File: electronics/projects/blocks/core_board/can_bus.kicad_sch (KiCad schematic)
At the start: 8 parts, among them U801 TCAN330DR

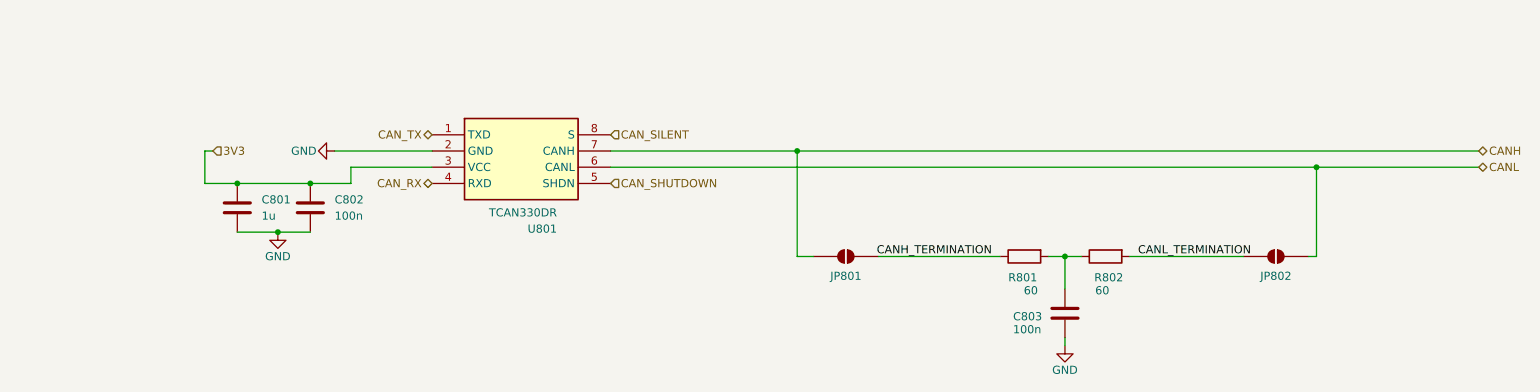
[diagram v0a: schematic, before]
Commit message: Update all sheets in core board project. Still looking for processes that give the cleanest update of a design block to a target board design.
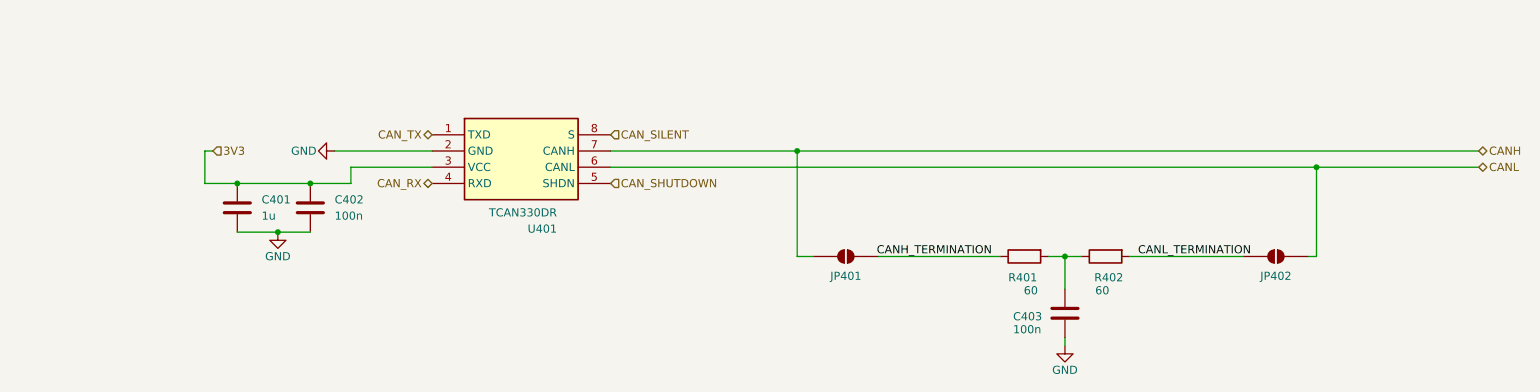
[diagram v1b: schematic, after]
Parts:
- renumbered C801 to C401, C802 to C402, C803 to C403, JP801 to JP401, JP802 to JP402, R801 to R401, R802 to R402, U801 to U401
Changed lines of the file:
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@@
 		(in_pos_files yes)
 		(dnp no)
-		(property "Reference" "C803"
+		(property "Reference" "C403"
 			(at 173.228 77.978 0)
 			(show_name no)
@@
 			)
 			(project "core_board"
-				(path "/efde0c74-5be6-4589-ad87-b4823ac1634b/c87fd2a4-f8d6-4149-89ef-17a7a7e4f014/68c0cd51-7ed2-4766-8be8-a243f7151f10"
-					(reference "C803")
+				(path "/efde0c74-5be6-4589-ad87-b4823ac1634b/c87fd2a4-f8d6-4149-89ef-17a7a7e4f014/66e88cae-c705-41c6-a86f-41a4af975dfd"
+					(reference "C403")
 					(unit 1)
 				)
@@
 		(in_pos_files yes)
 		(dnp no)
-		(property "Reference" "U801"
+		(property "Reference" "U401"
 			(at 99.568 64.262 0)
 			(show_name no)
@@
 			)
 			(project "core_board"
-				(path "/efde0c74-5be6-4589-ad87-b4823ac1634b/c87fd2a4-f8d6-4149-89ef-17a7a7e4f014/68c0cd51-7ed2-4766-8be8-a243f7151f10"
-					(reference "U801")
+				(path "/efde0c74-5be6-4589-ad87-b4823ac1634b/c87fd2a4-f8d6-4149-89ef-17a7a7e4f014/66e88cae-c705-41c6-a86f-41a4af975dfd"
+					(reference "U401")
 					(unit 1)
 				)
@@
 		(in_pos_files yes)
 		(dnp no)
-		(property "Reference" "R802"
+		(property "Reference" "R402"
 			(at 185.928 71.882 90)
 			(show_name no)
@@
 			)
 			(project "core_board"
-				(path "/efde0c74-5be6-4589-ad87-b4823ac1634b/c87fd2a4-f8d6-4149-89ef-17a7a7e4f014/68c0cd51-7ed2-4766-8be8-a243f7151f10"
-					(reference "R802")
+				(path "/efde0c74-5be6-4589-ad87-b4823ac1634b/c87fd2a4-f8d6-4149-89ef-17a7a7e4f014/66e88cae-c705-41c6-a86f-41a4af975dfd"
+					(reference "R402")
 					(unit 1)
 				)
@@
 		(in_pos_files yes)
 		(dnp no)
-		(property "Reference" "#PWR0802"
+		(property "Reference" "#PWR0402"
 			(at 58.42 52.07 0)
 			(hide yes)
@@
 			)
 			(project "core_board"
-				(path "/efde0c74-5be6-4589-ad87-b4823ac1634b/c87fd2a4-f8d6-4149-89ef-17a7a7e4f014/68c0cd51-7ed2-4766-8be8-a243f7151f10"
-					(reference "#PWR0802")
+				(path "/efde0c74-5be6-4589-ad87-b4823ac1634b/c87fd2a4-f8d6-4149-89ef-17a7a7e4f014/66e88cae-c705-41c6-a86f-41a4af975dfd"
+					(reference "#PWR0402")
 					(unit 1)
 				)
@@
 		(in_pos_files yes)
 		(dnp no)
-		(property "Reference" "JP801"
+		(property "Reference" "JP401"
 			(at 144.78 72.39 0)
 			(show_name no)
@@
 			)
 			(project "core_board"
-				(path "/efde0c74-5be6-4589-ad87-b4823ac1634b/c87fd2a4-f8d6-4149-89ef-17a7a7e4f014/68c0cd51-7ed2-4766-8be8-a243f7151f10"
-					(reference "JP801")
+				(path "/efde0c74-5be6-4589-ad87-b4823ac1634b/c87fd2a4-f8d6-4149-89ef-17a7a7e4f014/66e88cae-c705-41c6-a86f-41a4af975dfd"
+					(reference "JP401")
 					(unit 1)
 				)
@@
 		(in_pos_files yes)
 		(dnp no)
-		(property "Reference" "#PWR0801"
+		(property "Reference" "#PWR0401"
 			(at 55.88 71.12 0)
 			(hide yes)
@@
 			)
 			(project "core_board"
-				(path "/efde0c74-5be6-4589-ad87-b4823ac1634b/c87fd2a4-f8d6-4149-89ef-17a7a7e4f014/68c0cd51-7ed2-4766-8be8-a243f7151f10"
-					(reference "#PWR0801")
+				(path "/efde0c74-5be6-4589-ad87-b4823ac1634b/c87fd2a4-f8d6-4149-89ef-17a7a7e4f014/66e88cae-c705-41c6-a86f-41a4af975dfd"
+					(reference "#PWR0401")
 					(unit 1)
 				)
@@
 		(in_pos_files yes)
 		(dnp no)
-		(property "Reference" "#PWR0803"
+		(property "Reference" "#PWR0403"
 			(at 179.07 88.9 0)
 			(hide yes)
@@
 			)
 			(project "core_board"
-				(path "/efde0c74-5be6-4589-ad87-b4823ac1634b/c87fd2a4-f8d6-4149-89ef-17a7a7e4f014/68c0cd51-7ed2-4766-8be8-a243f7151f10"
-					(reference "#PWR0803")
+				(path "/efde0c74-5be6-4589-ad87-b4823ac1634b/c87fd2a4-f8d6-4149-89ef-17a7a7e4f014/66e88cae-c705-41c6-a86f-41a4af975dfd"
+					(reference "#PWR0403")
 					(unit 1)
 				)
@@
 		(in_pos_files yes)
 		(dnp no)
-		(property "Reference" "JP802"
+		(property "Reference" "JP402"
 			(at 212.09 72.39 0)
 			(show_name no)
@@
 			)
 			(project "core_board"
-				(path "/efde0c74-5be6-4589-ad87-b4823ac1634b/c87fd2a4-f8d6-4149-89ef-17a7a7e4f014/68c0cd51-7ed2-4766-8be8-a243f7151f10"
-					(reference "JP802")
+				(path "/efde0c74-5be6-4589-ad87-b4823ac1634b/c87fd2a4-f8d6-4149-89ef-17a7a7e4f014/66e88cae-c705-41c6-a86f-41a4af975dfd"
+					(reference "JP402")
 					(unit 1)
 				)
@@
 		(dnp no)
 		(fields_autoplaced yes)
-		(property "Reference" "C802"
+		(property "Reference" "C402"
 			(at 64.77 59.69 0)
 			(show_name no)
@@
 			)
 			(project "core_board"
-				(path "/efde0c74-5be6-4589-ad87-b4823ac1634b/c87fd2a4-f8d6-4149-89ef-17a7a7e4f014/68c0cd51-7ed2-4766-8be8-a243f7151f10"
-					(reference "C802")
+				(path "/efde0c74-5be6-4589-ad87-b4823ac1634b/c87fd2a4-f8d6-4149-89ef-17a7a7e4f014/66e88cae-c705-41c6-a86f-41a4af975dfd"
+					(reference "C402")
 					(unit 1)
 				)
@@
 		(in_pos_files yes)
 		(dnp no)
-		(property "Reference" "R801"
+		(property "Reference" "R401"
 			(at 172.466 71.882 90)
 			(show_name no)
@@
 			)
 			(project "core_board"
-				(path "/efde0c74-5be6-4589-ad87-b4823ac1634b/c87fd2a4-f8d6-4149-89ef-17a7a7e4f014/68c0cd51-7ed2-4766-8be8-a243f7151f10"
-					(reference "R801")
+				(path "/efde0c74-5be6-4589-ad87-b4823ac1634b/c87fd2a4-f8d6-4149-89ef-17a7a7e4f014/66e88cae-c705-41c6-a86f-41a4af975dfd"
+					(reference "R401")
 					(unit 1)
 				)
@@
 		(dnp no)
 		(fields_autoplaced yes)
-		(property "Reference" "C801"
+		(property "Reference" "C401"
 			(at 53.34 59.69 0)
 			(show_name no)
@@
 			)
 			(project "core_board"
-				(path "/efde0c74-5be6-4589-ad87-b4823ac1634b/c87fd2a4-f8d6-4149-89ef-17a7a7e4f014/68c0cd51-7ed2-4766-8be8-a243f7151f10"
-					(reference "C801")
-					(unit 1)
-				)
+				(path "/efde0c74-5be6-4589-ad87-b4823ac1634b/c87fd2a4-f8d6-4149-89ef-17a7a7e4f014/66e88cae-c705-41c6-a86f-41a4af975dfd"
+					(reference "C401")
+					(unit 1)
+				)

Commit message: Get core board schematic and layout to pass ERC and DRC. Rework layout to improve organization of components while allowing for future reuse of design.
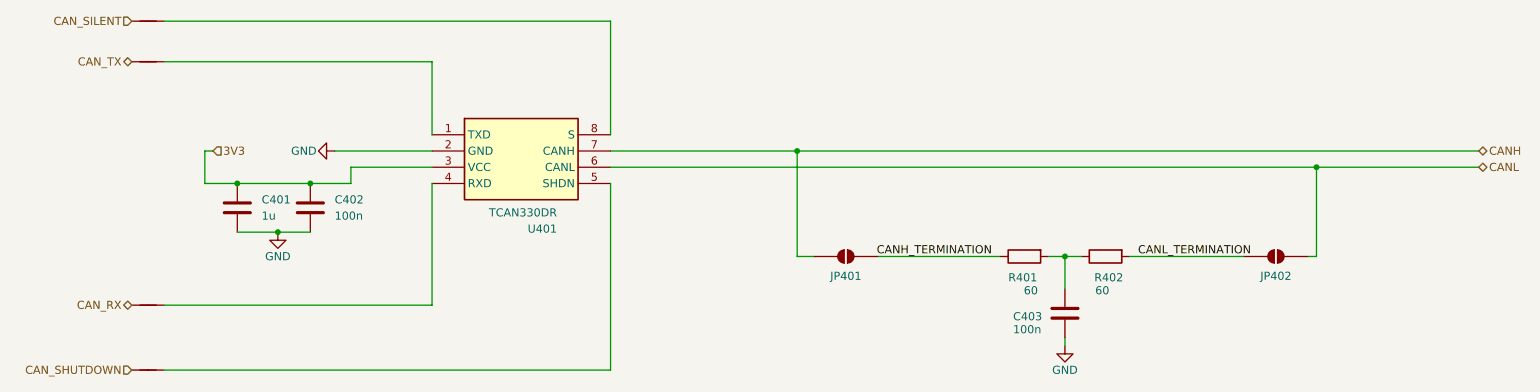
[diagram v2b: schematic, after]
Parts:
- added NT401, NT402, NT403, NT404: NetTie_2, NetTie:NetTie-2_SMD_Pad0.5mm, symbol Device:NetTie_2
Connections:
- net CAN_RX: now also NT403.1; no longer U401.4 (RXD)
- net CAN_SHUTDOWN: now also NT404.1; no longer U401.5 (SHDN)
- net CAN_SILENT: now also NT401.1; no longer U401.8 (S)
- net CAN_TX: now also NT402.1; no longer U401.1 (TXD)
- new net: NT402.2, U401.1 (TXD)
- new net: NT403.2, U401.4 (RXD)
- new net: NT404.2, U401.5 (SHDN)
- new net: NT401.2, U401.8 (S)
